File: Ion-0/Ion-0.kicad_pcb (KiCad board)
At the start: 2 copper layers, 99 parts, among them J1 Beaglebone-green-P9, J10 Conn_Heater, J11 Conn_01x02, J12 Conn_01x02, J13 Conn_01x04, J2 Beaglebone-green-P8, J3 Conn_02x06_Odd_Even, J4 Conn_02x06_Odd_Even, J5 Conn_02x06_Odd_Even, J6 Coaxial_Small, J7 Conn_01x02, J8 Conn_Heater, J9 Conn_Heater, Q1 IRLML6244, Q2 IRLML6244, Q3 IRLML6244, Q4 IRLML6244, U2 LMT84DCK, U3 BNO085, U4 TCA9617ADGKR, U5 LMT84DCK, U6 MAX-M10M-00B, U7 TPS3850H50DRCR, U8 SN65HVD230, U9 MS860702BA01-50, Y2 9HT10-32.768KBZF-T

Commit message: init commit for layout
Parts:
- J13, J3, J4, J5: moved to B.Cu
- moved J1 119.3 mm to (88.3, 80.2)
- moved C11 114.8 mm to (59.1, 177.0), turned to -90 degrees
- moved U3 108.3 mm to (42.8, 150.2), turned to 90 degrees
- moved Q2 103.4 mm to (37.6, 171.8)
- moved Q3 96.9 mm to (49.9, 174.4), turned to 90 degrees
- moved U4 93.4 mm to (60.2, 159.8)
- moved J7 92.0 mm to (109.9, 144.4)
- moved L1 78.0 mm to (62.0, 177.9)
- moved J6 74.6 mm to (101.4, 63.1)
- moved J5 71.8 mm to (95.3, 123.2), turned to 180 degrees
- moved J11 69.3 mm to (80.0, 131.6), turned to -90 degrees
- moved U8 65.5 mm to (53.2, 138.1)
- moved J12 64.0 mm to (80.1, 124.5), turned to -90 degrees
- moved Y2 60.9 mm to (50.1, 152.5)
- moved J13 53.6 mm to (101.0, 145.6), turned to 180 degrees
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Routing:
- net /AIN0: track 0.00 -> 7.13 mm
- net /AIN2: track 0.00 -> 6.96 mm
- net Net-(J8-Pin_2): track 0.00 -> 5.57 mm
- net +5V: track 0.00 -> 2.63 mm
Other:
- copper layers 2 -> 4

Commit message: midway through
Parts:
- C1, C10, C11, C12, C13, C14, C15, C16, C17, C18, C19, C2, C20, C21, C22, C3, C4, C5, C6, C7, C8, C9: footprint Capacitor_SMD:C_0201_0603Metric -> Capacitor_SMD:C_0603_1608Metric
- D7, D8, D9: footprint Diode_SMD:D_SMB -> Diode_SMD:D_0402_1005Metric_Pad0.77x0.64mm_HandSolder
- J13, J3, J4, J5: moved to F.Cu
- JP1, JP2, JP3, JP4, R16, U2, U4: moved to B.Cu
- moved R32 149.4 mm to (129.3, 156.6), turned to -90 degrees
- moved R33 145.6 mm to (126.2, 156.6), turned to -90 degrees
- moved R31 142.2 mm to (135.0, 156.7), turned to -90 degrees
- moved R30 142.2 mm to (132.3, 156.6), turned to -90 degrees
- moved R34 141.8 mm to (123.2, 156.6), turned to -90 degrees
- moved R16 141.3 mm to (121.7, 150.6), turned to -90 degrees
- moved R35 130.9 mm to (101.9, 159.2), turned to 90 degrees
- moved R18 130.5 mm to (111.9, 149.6), turned to -90 degrees
- moved D2 124.8 mm to (132.3, 161.1), turned to 90 degrees
- moved D3 124.0 mm to (135.3, 161.1), turned to 90 degrees
- moved D1 123.7 mm to (122.0, 134.4), turned to 90 degrees
- moved R36 122.8 mm to (101.9, 152.5), turned to -90 degrees
- moved R37 122.4 mm to (101.0, 155.1), turned to 180 degrees
- moved R38 121.5 mm to (101.0, 156.6), turned to 180 degrees
- moved D4 118.1 mm to (129.3, 161.1), turned to 90 degrees
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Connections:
- D1 pad 1: /Sensor-bus-hat/CAN_P -> /Sensor-bus-hat/CAN_N
- D1 pad 2: /Sensor-bus-hat/CAN_N -> /Sensor-bus-hat/CAN_P
- J1 pad 12: unconnected-(J1-Pin_12-Pad12) -> /GPIO_60
- J1 pad 14: unconnected-(J1-Pin_14-Pad14) -> /GPIO_50
- J2 pad 3: /GPIO_38 -> unconnected-(J2-Pin_3-Pad3)
- J2 pad 5: /GPIO_34 -> unconnected-(J2-Pin_5-Pad5)
- J7 pad 1: /Sensor-bus-hat/CAN_P -> /Sensor-bus-hat/CAN_N
- J7 pad 2: /Sensor-bus-hat/CAN_N -> /Sensor-bus-hat/CAN_P
- R14 pad 2: /GPIO_38 -> /GPIO_60
- R33 pad 1: /GPIO_76 -> /GPIO_74
- R34 pad 1: /GPIO_74 -> /GPIO_76
- U7 pad 7: /GPIO_34 -> /GPIO_50
- U7 pad 9: /GPIO_38 -> /GPIO_60
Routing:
- net /I2C1_SDA: track 0.00 -> 111.0 mm, vias 0 -> 3
- net /I2C1_SCL: track 0.00 -> 108.8 mm, vias 0 -> 3
- net +5V: track 2.63 -> 92.0 mm, vias 0 -> 4
- net Net-(U4-SDAB): track 0.00 -> 61.0 mm, vias 0 -> 1
- net Net-(U4-SCLB): track 0.00 -> 58.5 mm, vias 0 -> 1
- net /Sensor-bus-hat/CAN_P: track 0.00 -> 54.7 mm
- net /I2C2_SCL: track 0.00 -> 53.3 mm, vias 0 -> 1
- net /Sensor-bus-hat/CAN_N: track 0.00 -> 52.2 mm
- net /I2C2_SDA: track 0.00 -> 46.1 mm, vias 0 -> 1
- net /AIN2: track 6.96 -> 51.8 mm
- net /AIN0: track 7.13 -> 47.0 mm
- net /GPIO_76: track 0.00 -> 32.9 mm, vias 0 -> 1
- net /GPIO_74: track 0.00 -> 29.0 mm, vias 0 -> 1
- net /GPIO_72: track 0.00 -> 25.2 mm, vias 0 -> 1
- net Net-(Q2-G): track 0.00 -> 17.9 mm
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- added copper zone on In2.Cu, net +3V3
- added copper zone on In2.Cu, net +5V
- added copper zone on B.Cu, net GND
- added copper zone on F.Cu, net GND
- added copper zone on In1.Cu, net GND
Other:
- board outline added: 54.6 x 97.2 mm

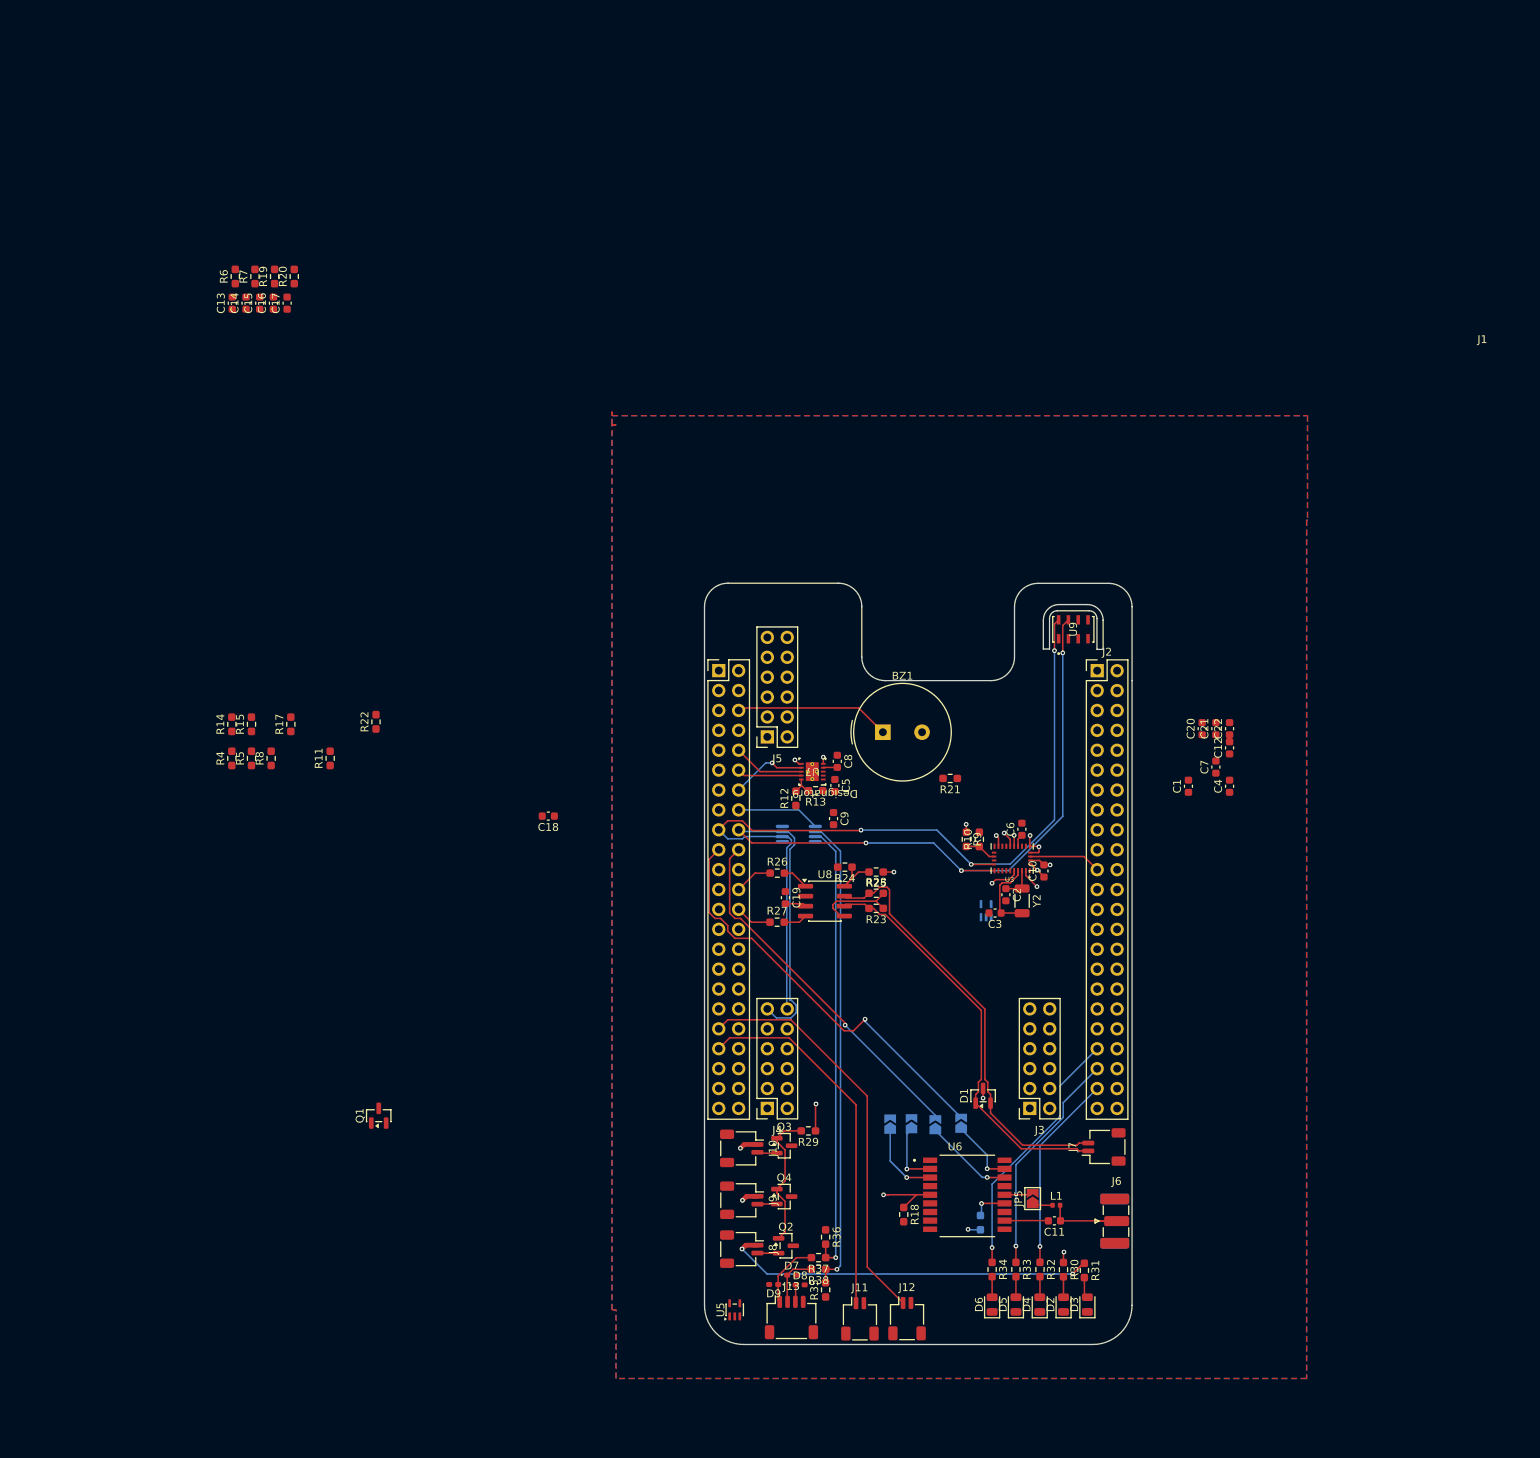
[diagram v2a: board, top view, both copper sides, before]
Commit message: finished tracing, need to fix m3 holes, text, impedance match antenna, via stiching
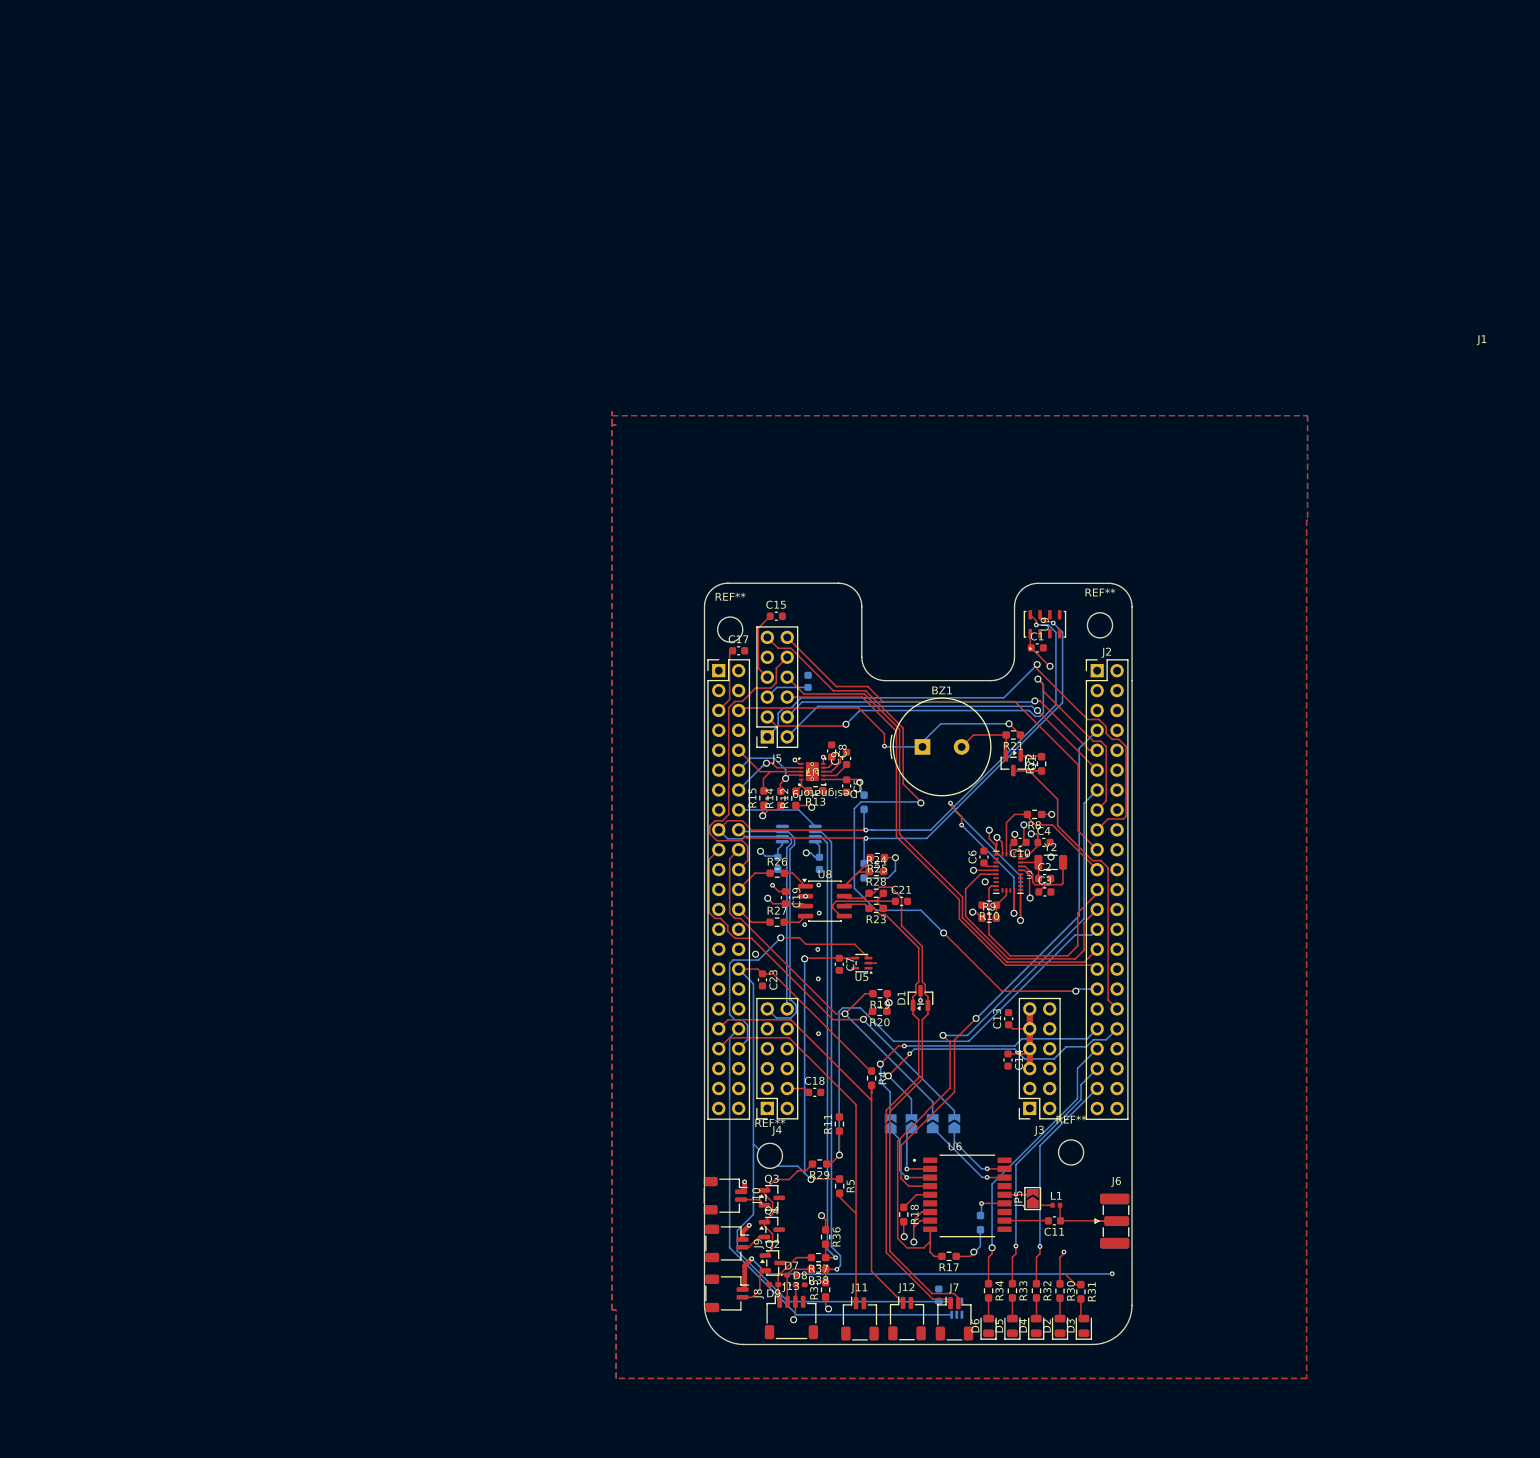
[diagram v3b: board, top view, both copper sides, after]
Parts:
- added C23: 1uF, Capacitor_SMD:C_0603_1608Metric, F.Cu at (93.9, 119.7)
- added REF**: MountingHole_3.2mm_M3, MountingHole:MountingHole_3.2mm_M3, F.Cu at (89.8, 74.9)
- added REF**: MountingHole_3.2mm_M3, MountingHole:MountingHole_3.2mm_M3, F.Cu at (137.0, 74.4)
- added REF**: MountingHole_3.2mm_M3, MountingHole:MountingHole_3.2mm_M3, F.Cu at (133.3, 141.7)
- added REF**: MountingHole_3.2mm_M3, MountingHole:MountingHole_3.2mm_M3, F.Cu at (94.8, 142.1)
- C12, C16, C20, C22, R6, R7: moved to B.Cu
- moved C14 137.1 mm to (125.2, 129.9), turned to -90 degrees
- moved C13 134.8 mm to (125.3, 124.6)
- moved R20 119.9 mm to (108.8, 123.7), turned to 180 degrees
- moved R19 119.8 mm to (108.9, 121.4), turned to 180 degrees
- moved R6 110.4 mm to (106.9, 105.7), turned to -90 degrees
- moved R17 108.0 mm to (117.7, 154.9), turned to 180 degrees
- moved R7 102.7 mm to (106.8, 97.0), turned to -90 degrees
- moved R8 97.7 mm to (128.6, 98.5), turned to 180 degrees
- moved R5 92.8 mm to (103.7, 146.0), turned to -90 degrees
- moved Q1 92.7 mm to (125.9, 92.0), turned to -90 degrees
- moved R4 91.3 mm to (107.8, 132.2), turned to -90 degrees
- moved R22 85.1 mm to (129.5, 92.1)
- moved C16 83.6 mm to (99.7, 81.5)
- moved C22 81.3 mm to (116.4, 159.9)
- moved R11 80.0 mm to (103.7, 138.1)
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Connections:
- J1 pad 11: /UART4_RXD -> unconnected-(J1-Pin_11-Pad11)
- J1 pad 13: /UART4_TXD -> unconnected-(J1-Pin_13-Pad13)
- J2 pad 37: unconnected-(J2-Pin_37-Pad37) -> /UART4_TXD
- J2 pad 38: unconnected-(J2-Pin_38-Pad38) -> /UART4_RXD
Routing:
- net +1V8: track 0.00 -> 136.8 mm, vias 0 -> 2
- net +3V3: track 15.6 -> 112.3 mm, vias 6 -> 20
- net /IND_3: track 0.00 -> 88.2 mm, vias 0 -> 3
- net /GPIO_69: track 0.00 -> 80.0 mm, vias 0 -> 1
- net /Timer4: track 0.00 -> 71.7 mm, vias 0 -> 1
- net /SERVO_2: track 0.00 -> 69.1 mm, vias 0 -> 1
- net /MOTOR_2_A: track 0.00 -> 64.7 mm
- net /MOTOR_2_B: track 0.00 -> 63.3 mm
- net /SERVO_1: track 0.00 -> 63.0 mm, vias 0 -> 2
- net /GPIO_86: track 3.46 -> 64.4 mm
- net /AIN3: track 0.00 -> 60.3 mm
- net /LED_PWM_2: track 0.00 -> 55.7 mm
- net /MOTOR_1_B: track 0.00 -> 44.6 mm, vias 0 -> 1
- net /MOTOR_1_A: track 0.00 -> 43.0 mm, vias 0 -> 1
- net /UART4_RXD: track 0.00 -> 39.4 mm, vias 0 -> 2
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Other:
- outline, holes or cut-outs redrawn

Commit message: restarting layout
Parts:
- removed BZ1: PS1240P02BT, Buzzer_Beeper:Buzzer_TDK_PS1240P02BT_D12.2mm_H6.5mm
- removed C1: 220nF, Capacitor_SMD:C_0603_1608Metric
- removed C10, C12, C13, C15, C18, C19, C20: 100nF, Capacitor_SMD:C_0603_1608Metric
- removed C11: 47pF, Capacitor_SMD:C_0603_1608Metric
- removed C14, C16, C17: 22uF, Capacitor_SMD:C_0603_1608Metric
- removed C2, C3: 22pF, Capacitor_SMD:C_0603_1608Metric
- removed C21: 4.7nF, Capacitor_SMD:C_0603_1608Metric
- removed C22, C23, C7, C8: 1uF, Capacitor_SMD:C_0603_1608Metric
- removed C4, C5, C6: 0.1uF, Capacitor_SMD:C_0603_1608Metric
- removed C9: 100pF, Capacitor_SMD:C_0603_1608Metric
- removed D1: ESD3V3T2BHE3, Package_TO_SOT_SMD:SOT-23
- removed D2, D3, D4, D5, D6: LED, LED_SMD:LED_0805_2012Metric
- removed D7, D8, D9: TVS_3V3, Diode_SMD:D_0402_1005Metric_Pad0.77x0.64mm_HandSolder
- removed J1: Beaglebone-green-P9, Connector_PinHeader_2.54mm:PinHeader_2x23_P2.54mm_Vertical
- removed J10, J8, J9: Conn_Heater, Connector_JST:JST_SH_SM02B-SRSS-TB_1x02-1MP_P1.00mm_Horizontal
- removed J11, J12, J7: Conn_01x02, Connector_JST:JST_SH_SM02B-SRSS-TB_1x02-1MP_P1.00mm_Horizontal
- removed J13: Conn_01x04, Connector_JST:JST_SH_SM04B-SRSS-TB_1x04-1MP_P1.00mm_Horizontal
- removed J2: Beaglebone-green-P8, Connector_PinHeader_2.54mm:PinHeader_2x23_P2.54mm_Vertical
- removed J3, J4, J5: Conn_02x06_Odd_Even, Connector_PinSocket_2.54mm:PinSocket_2x06_P2.54mm_Vertical
- removed J6: Coaxial_Small, Connector_Coaxial:SMA_Samtec_SMA-J-P-H-ST-EM1_EdgeMount
- removed JP1, JP2, JP3, JP4, JP5: SolderJumper_2_Open, Jumper:SolderJumper-2_P1.3mm_Open_TrianglePad1.0x1.5mm
- removed L1: 101nH, Inductor_SMD:L_0402_1005Metric
- removed Q1, Q2, Q3, Q4: IRLML6244, Package_TO_SOT_SMD:SOT-23
- removed R10, R24: 0, Resistor_SMD:R_0603_1608Metric_Pad0.98x0.95mm_HandSolder
- removed R11, R14, R15, R16, R17, R35, R36, R8: 10K, Resistor_SMD:R_0603_1608Metric_Pad0.98x0.95mm_HandSolder
- removed R12: 523, Resistor_SMD:R_0603_1608Metric_Pad0.98x0.95mm_HandSolder
- removed R13: 80.6, Resistor_SMD:R_0603_1608Metric_Pad0.98x0.95mm_HandSolder
- removed R18, R19, R20, R6, R7: 4.7K, Resistor_SMD:R_0603_1608Metric_Pad0.98x0.95mm_HandSolder
- removed R21, R22, R29, R32, R33, R34, R37, R38: 330, Resistor_SMD:R_0603_1608Metric_Pad0.98x0.95mm_HandSolder
- removed R23, R28: 60, Resistor_SMD:R_0603_1608Metric_Pad0.98x0.95mm_HandSolder
- removed R25, R9: DNI, Resistor_SMD:R_0603_1608Metric_Pad0.98x0.95mm_HandSolder
- removed R26, R27: 33, Resistor_SMD:R_0603_1608Metric_Pad0.98x0.95mm_HandSolder
- removed R30: 470, Resistor_SMD:R_0603_1608Metric_Pad0.98x0.95mm_HandSolder
- removed R31: 1k, Resistor_SMD:R_0603_1608Metric_Pad0.98x0.95mm_HandSolder
- removed R4, R5: 100K, Resistor_SMD:R_0603_1608Metric_Pad0.98x0.95mm_HandSolder
- removed the REF** at (89.8, 74.9)
- removed the REF** at (137.0, 74.4)
- removed the REF** at (133.3, 141.7)
- removed the REF** at (94.8, 142.1)
- removed U2, U5: LMT84DCK, Package_TO_SOT_SMD:SOT-353_SC-70-5
- removed U3: BNO085, 1_Ion:IC_BNO085
- removed U4: TCA9617ADGKR, 1_Ion:TCA9617A
- removed U6: MAX-M10M-00B, 1_Ion:XCVR_MAX-M10M-00B
- removed U7: TPS3850H50DRCR, 1_Ion:TPS3850
- removed U8: SN65HVD230, Package_SO:SOIC-8_3.9x4.9mm_P1.27mm
- removed U9: MS860702BA01-50, 1_Ion:MS860702BA01-50_TEC
- removed Y2: 9HT10-32.768KBZF-T, Inductor_SMD:L_1206_3216Metric
- added REF**: MountingHole_3.2mm_M3_DIN965_Pad, MountingHole:MountingHole_3.2mm_M3_DIN965_Pad, F.Cu at (124.3, 72.0)
- added REF**: MountingHole_3.2mm_M3_DIN965_Pad, MountingHole:MountingHole_3.2mm_M3_DIN965_Pad, F.Cu at (169.4, 138.0)
- added REF**: MountingHole_3.2mm_M3_DIN965_Pad, MountingHole:MountingHole_3.2mm_M3_DIN965_Pad, F.Cu at (127.5, 138.0)
- added REF**: MountingHole_3.2mm_M3_DIN965_Pad, MountingHole:MountingHole_3.2mm_M3_DIN965_Pad, F.Cu at (172.7, 72.0)
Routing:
- net +1V8: track 136.8 -> 0.00 mm, vias 2 -> 0
- net +5V: track 127.7 -> 0.00 mm, vias 6 -> 0
- net /I2C1_SDA: track 122.2 -> 0.00 mm, vias 3 -> 0
- net /I2C1_SCL: track 120.6 -> 0.00 mm, vias 5 -> 0
- net +3V3: track 112.3 -> 0.00 mm, vias 20 -> 0
- net /IND_3: track 88.2 -> 0.00 mm, vias 3 -> 0
- net /GPIO_69: track 80.0 -> 0.00 mm, vias 1 -> 0
- net /Timer4: track 71.7 -> 0.00 mm, vias 1 -> 0
- net /SERVO_2: track 69.1 -> 0.00 mm, vias 1 -> 0
- net /Sensor-bus-hat/CAN_P: track 68.9 -> 0.00 mm
- net /MOTOR_2_A: track 64.7 -> 0.00 mm
- net /Sensor-bus-hat/CAN_N: track 64.4 -> 0.00 mm
- net /GPIO_86: track 64.4 -> 0.00 mm, vias 1 -> 0
- net /MOTOR_2_B: track 63.3 -> 0.00 mm
- net /SERVO_1: track 63.0 -> 0.00 mm, vias 2 -> 0
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- removed copper zone on In2.Cu, net +3V3
- removed copper zone on In2.Cu, net +5V
- removed copper zone on B.Cu, net GND
- removed copper zone on F.Cu, net GND
- removed copper zone on In1.Cu, net GND
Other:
- board size 54.6 x 97.2 mm -> 54.6 x 86.4 mm
